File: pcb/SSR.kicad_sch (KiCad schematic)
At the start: 21 parts, among them J1 Conn_01x04, J2 IN_AC, J3 RESISTENCIA, U1 MOC3021M, U2 H11AA1, U3 4N25

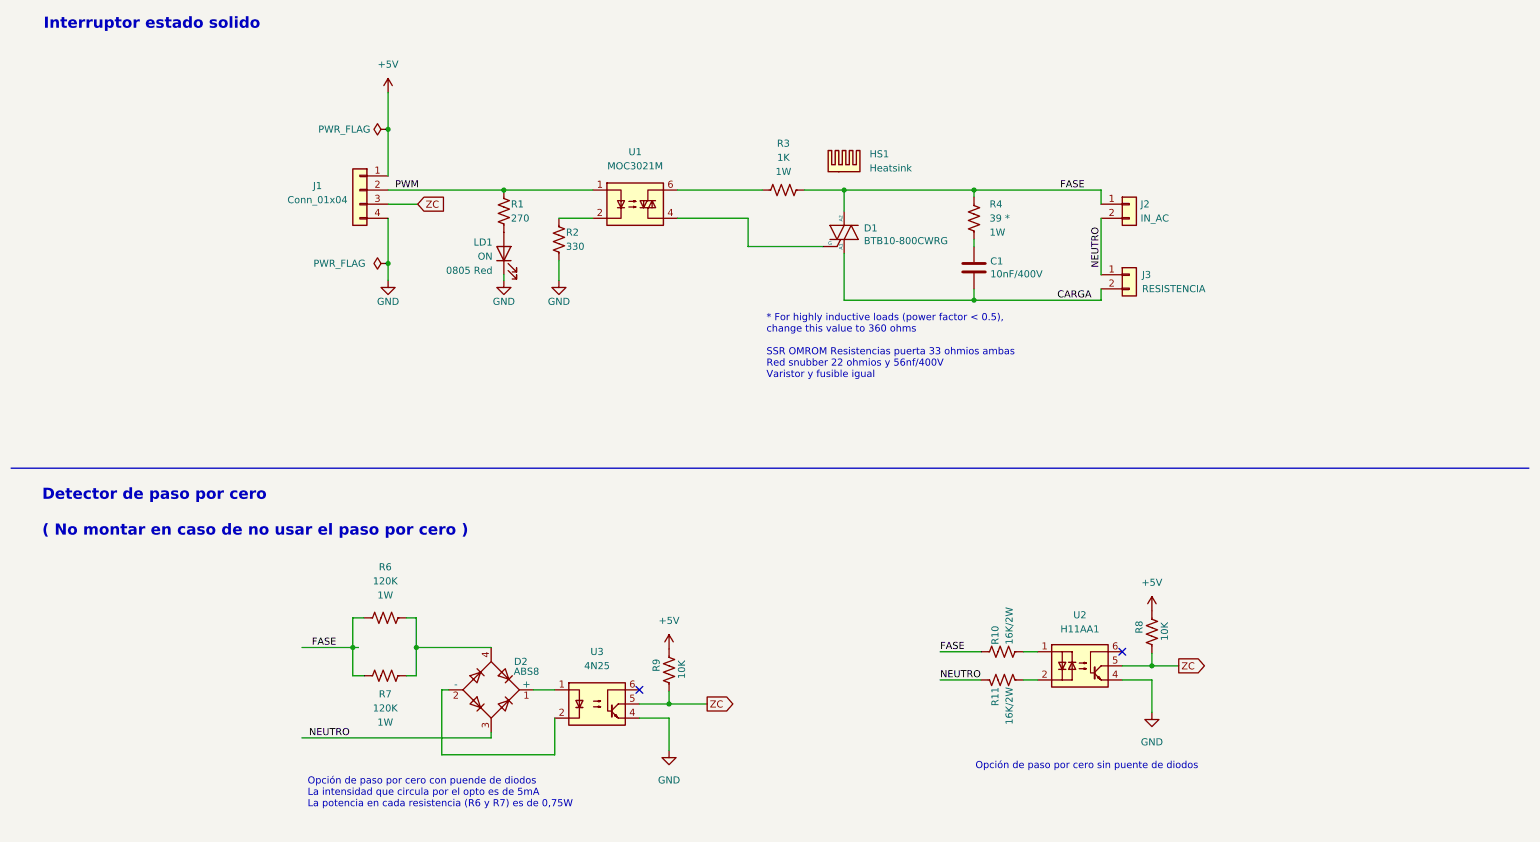
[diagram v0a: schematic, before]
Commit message: Añadido Zener
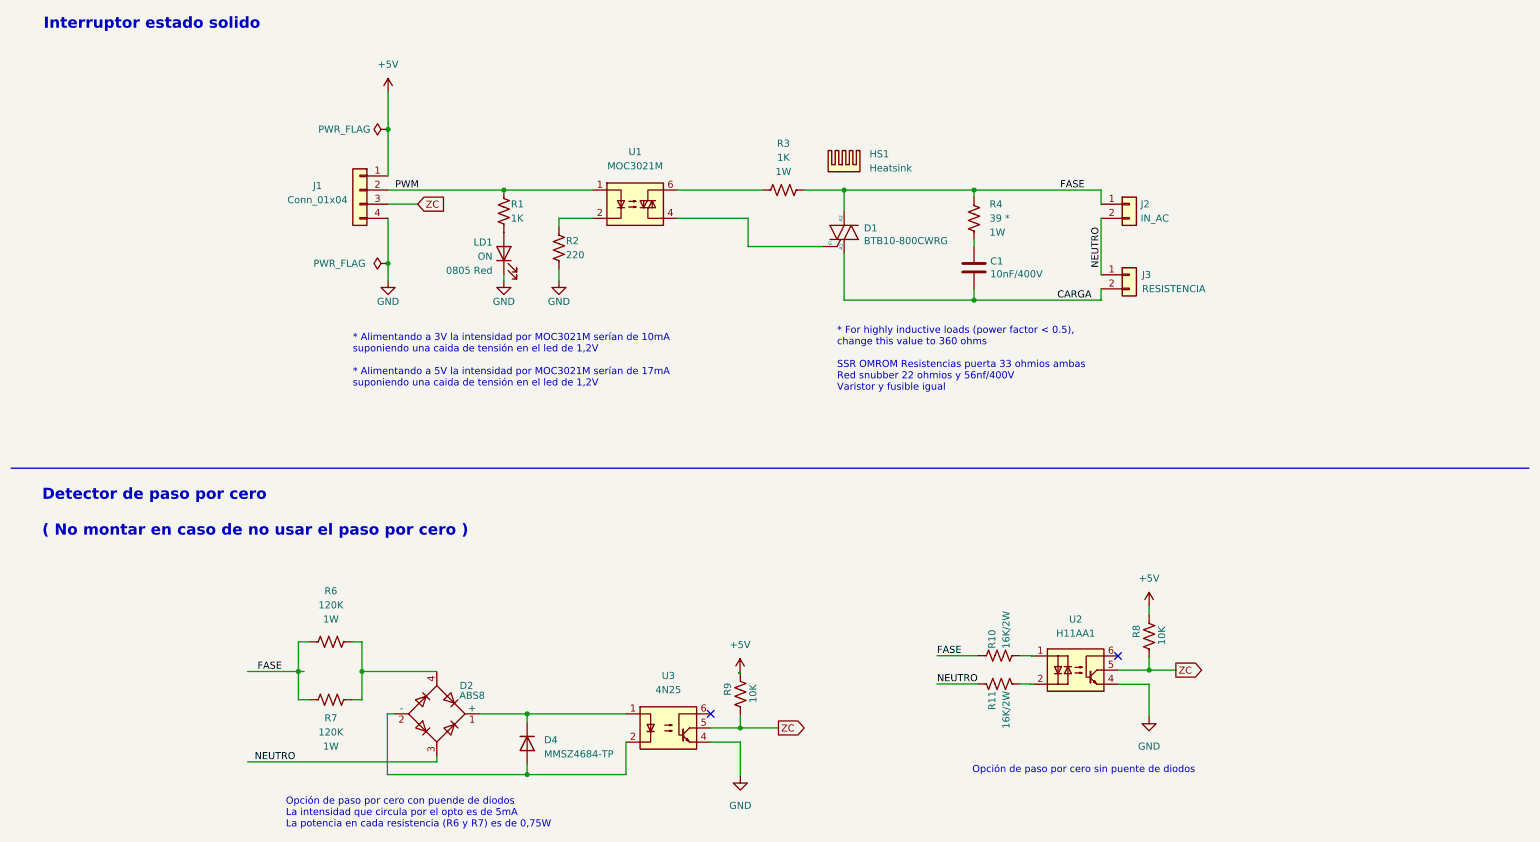
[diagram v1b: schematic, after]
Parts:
- added D4: MMSZ4684-TP, Diode_SMD:D_SOD-123, symbol Diode:US1M
- R1: value 270 -> 1K
- R2: value 330 -> 220
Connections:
- net at D2.1 (+), U3.1: now also D4.1 (K)
- net at D2.2 (-), U3.2: now also D4.2 (A)
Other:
- note added: "* Alimentando a 3V la intensidad por MOC3021M serían de 10mA suponiendo una caida de tensión en el led de 1,2V * Alimentando a 5V la intensidad por MOC3021M serían de 17mA suponiendo una caida de tensión en el led de 1,2V"
- moved on the sheet: D2, R10, R11, R2, R6, R7, R8, R9, U2, U3
